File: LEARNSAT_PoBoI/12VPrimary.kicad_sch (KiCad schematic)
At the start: 17 parts, among them Q3 SI7164DP-T1-GE3, U13 INA219AIDCNR, U18 LTC4231IUD-2#TRPBF

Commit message: Changed diode D?1 to D23 as a git test
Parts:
- renumbered D?1 to D23
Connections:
- net 12V_EnableP: now also D23.2 (A); no longer D23.1 (K)
- net GND: now also D23.1 (K); no longer D23.2 (A)

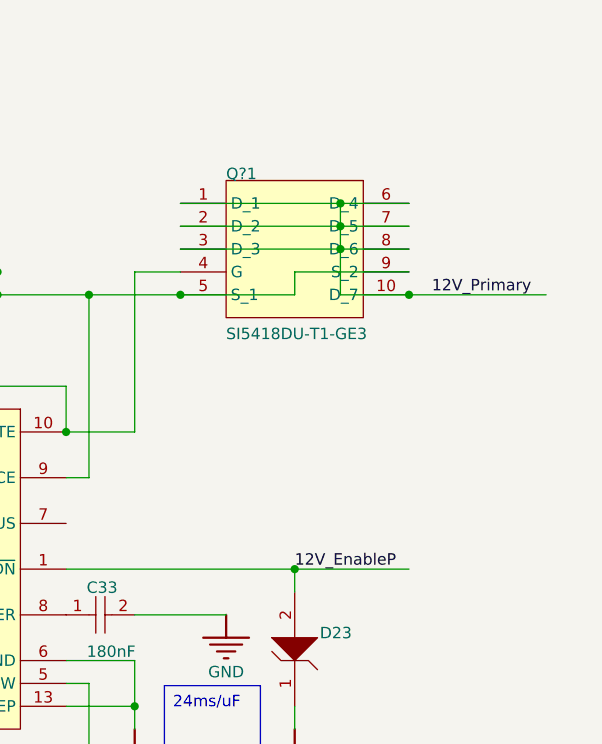
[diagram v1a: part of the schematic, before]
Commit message: Small global net changes
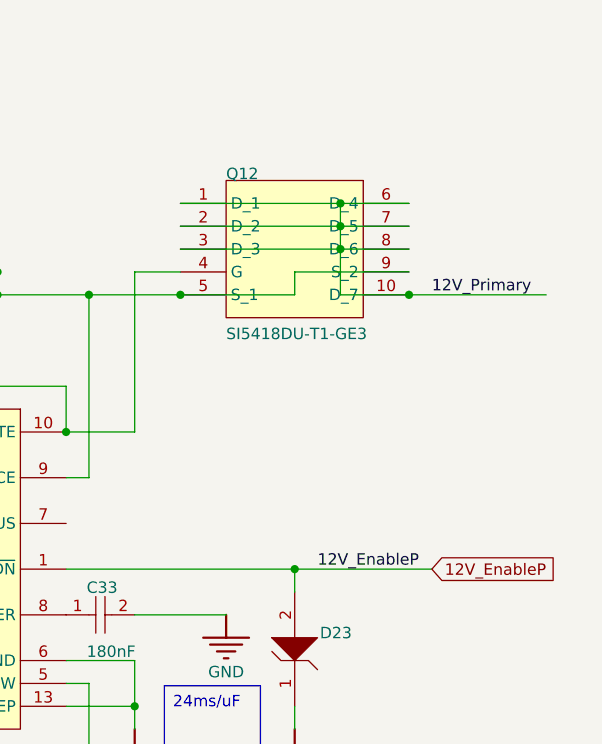
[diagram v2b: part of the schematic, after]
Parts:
- renumbered Q?1 to Q12
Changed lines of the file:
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@@
 	)
 	(junction
-		(at 167.64 149.86)
-		(diameter 0)
-		(color 0 0 0 0)
-	)
-	(junction
 		(at 99.06 45.72)
 		(diameter 0)
@@
 	)
 	(junction
+		(at 167.64 149.86)
+		(diameter 0)
+		(color 0 0 0 0)
+	)
+	(junction
 		(at 149.86 165.1)
 		(diameter 0)
@@
 	(wire
 		(pts
-			(xy 167.64 149.86) (xy 180.34 149.86)
+			(xy 167.64 149.86) (xy 182.88 149.86)
 		)
 		(stroke
@@
 	)
 	(label "12V_EnableP"
-		(at 167.64 149.86 0)
+		(at 170.18 149.86 0)
 		(effects
 			(font
@@
 		)
 	)
+	(global_label "12V_EnableP"
+		(shape input)
+		(at 182.88 149.86 0)
+		(fields_autoplaced yes)
+		(effects
+			(font
+				(size 1.27 1.27)
+			)
+			(justify left)
+		)
+		(property "Intersheetrefs" "${INTERSHEET_REFS}"
+			(at 197.9602 149.86 0)
+			(hide yes)
+			(show_name no)
+			(do_not_autoplace no)
+			(effects
+				(font
+					(size 1.27 1.27)
+				)
+				(justify left)
+			)
+		)
+	)
 	(symbol
 		(lib_id "UGA SSRL Hardware Team:root_0_94c330ae140e2337d879337fe7aaeec_UGA SSRL Hardware Team")
@@
 		(in_pos_files yes)
 		(dnp no)
-		(property "Reference" "Q?1"
+		(property "Reference" "Q12"
 			(at 160.02 106.68 0)
 			(show_name no)
@@
 			(project "LEARNSAT_POBOY_v3.2.0"
 				(path "/31302da5-a970-4b2b-aa05-afcd06cb9d09/2029a850-3e48-491b-a9aa-1537ac8442d4"
-					(reference "Q?1")
+					(reference "Q12")
 					(unit 1)
 				)

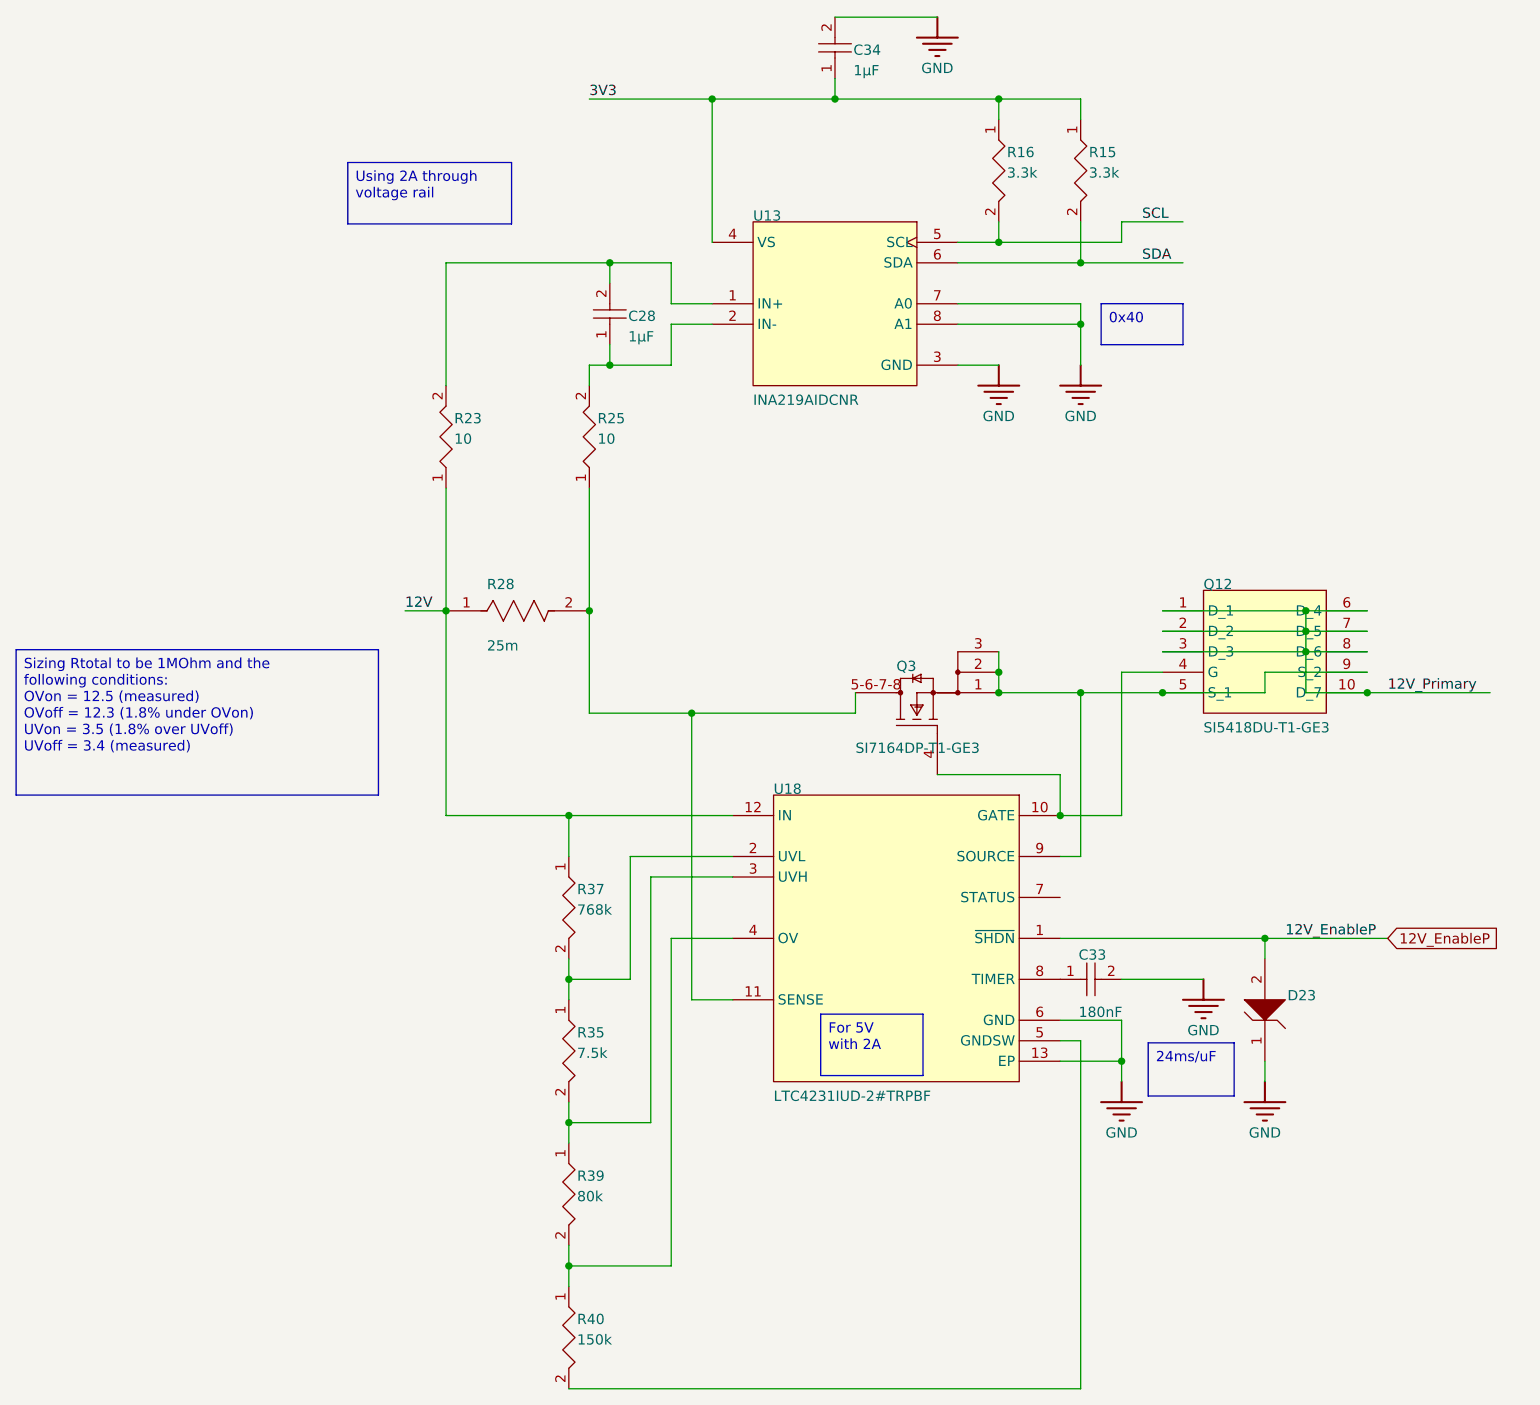
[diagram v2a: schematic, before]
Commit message: Replaced local nets with global and left local nets intact
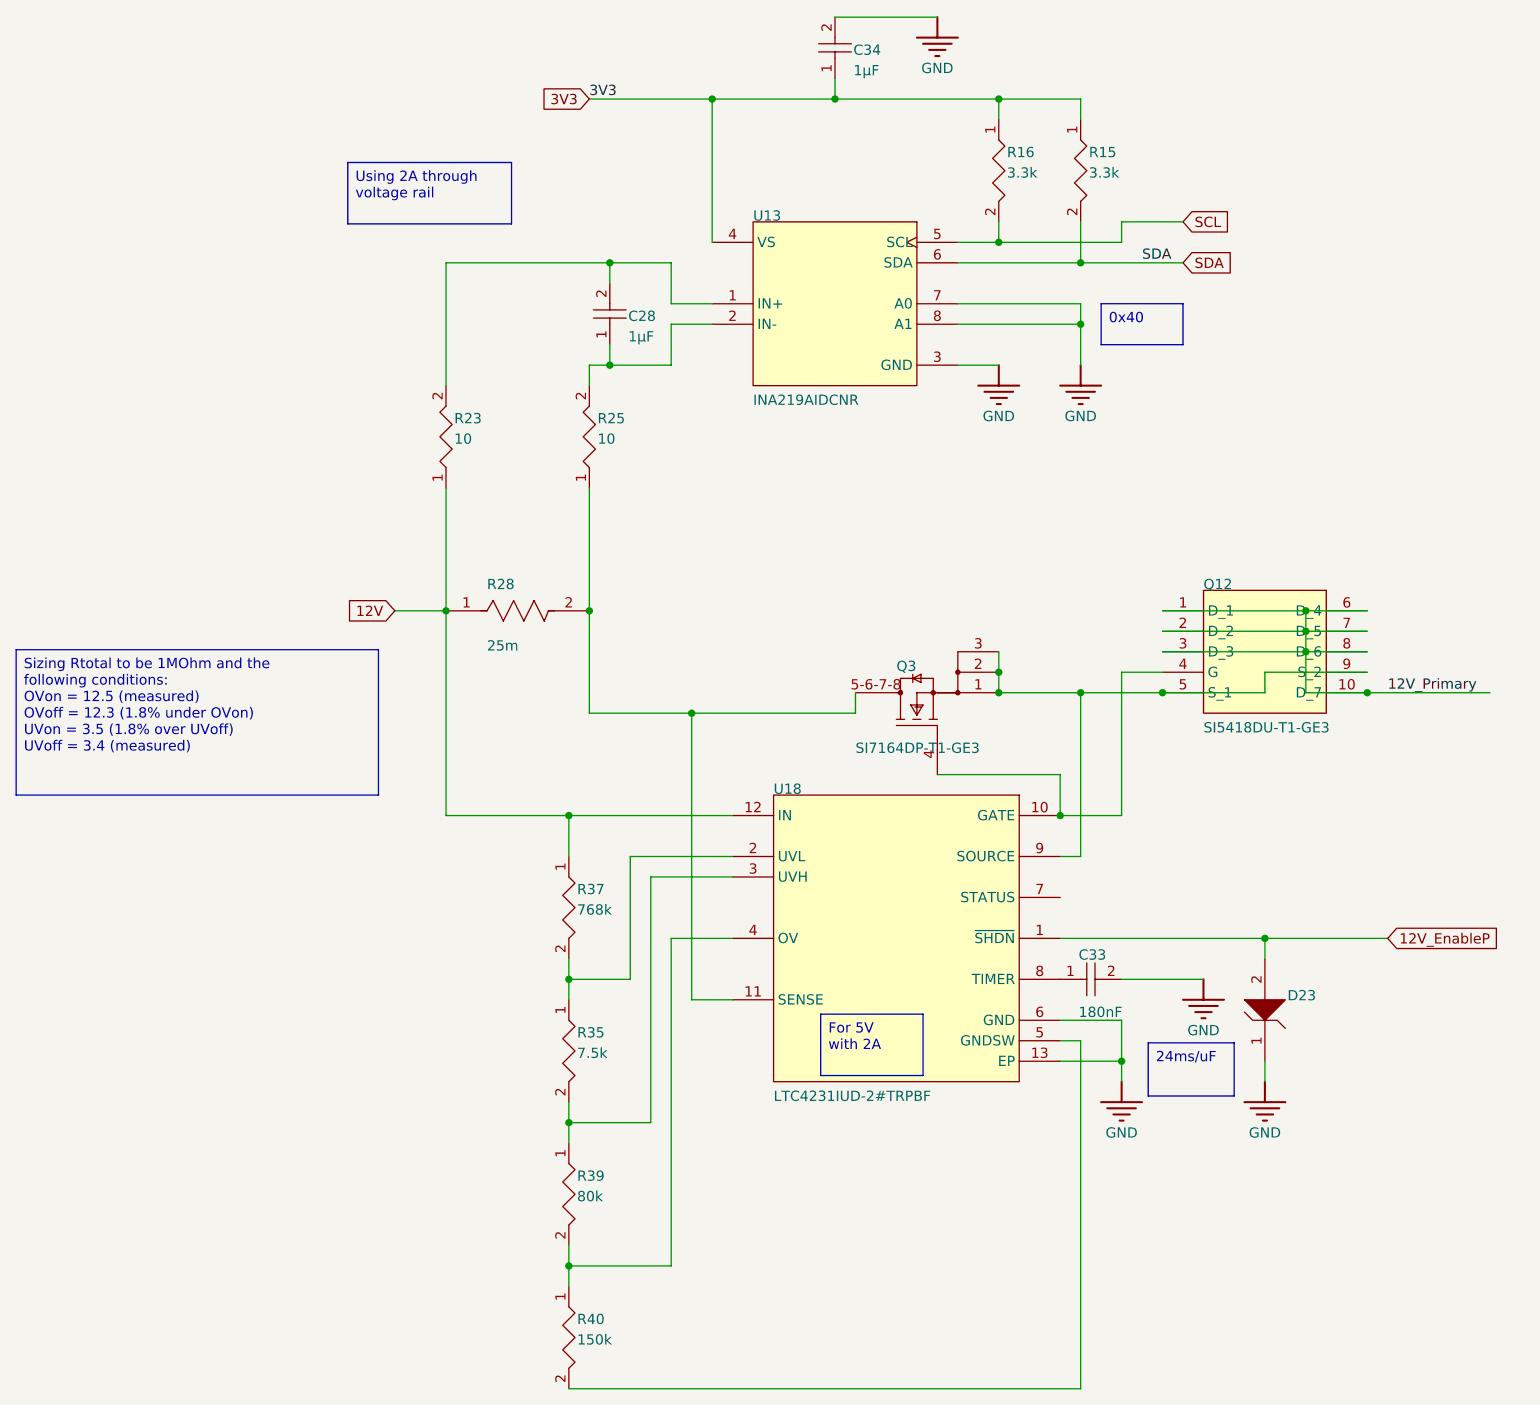
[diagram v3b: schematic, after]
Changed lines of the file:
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@@
 	(wire
 		(pts
-			(xy 60.96 109.22) (xy 66.04 109.22)
+			(xy 59.69 109.22) (xy 66.04 109.22)
 		)
 		(stroke
@@
 		)
 	)
-	(label "12V"
-		(at 60.96 109.22 0)
+	(label "SDA"
+		(at 152.4 66.04 0)
 		(effects
 			(font
@@
 		)
 	)
-	(label "SCL"
-		(at 152.4 60.96 0)
+	(label "3V3"
+		(at 83.82 45.72 0)
 		(effects
 			(font
@@
 		)
 	)
-	(label "SDA"
-		(at 152.4 66.04 0)
+	(label "12V_Primary"
+		(at 182.88 119.38 0)
 		(effects
 			(font
@@
 		)
 	)
-	(label "3V3"
-		(at 83.82 45.72 0)
+	(global_label "SCL"
+		(shape input)
+		(at 157.48 60.96 0)
+		(fields_autoplaced yes)
 		(effects
 			(font
 				(size 1.27 1.27)
 			)
-			(justify left bottom)
+			(justify left)
+		)
+		(property "Intersheetrefs" "${INTERSHEET_REFS}"
+			(at 163.9728 60.96 0)
+			(hide yes)
+			(show_name no)
+			(do_not_autoplace no)
+			(effects
+				(font
+					(size 1.27 1.27)
+				)
+				(justify left)
+			)
 		)
 	)
-	(label "12V_Primary"
-		(at 182.88 119.38 0)
+	(global_label "3V3"
+		(shape input)
+		(at 83.82 45.72 180)
+		(fields_autoplaced yes)
 		(effects
 			(font
 				(size 1.27 1.27)
 			)
-			(justify left bottom)
+			(justify right)
+		)
+		(property "Intersheetrefs" "${INTERSHEET_REFS}"
+			(at 77.3272 45.72 0)
+			(hide yes)
+			(show_name no)
+			(do_not_autoplace no)
+			(effects
+				(font
+					(size 1.27 1.27)
+				)
+				(justify right)
+			)
 		)
 	)
-	(label "12V_EnableP"
-		(at 170.18 149.86 0)
+	(global_label "SDA"
+		(shape input)
+		(at 157.48 66.04 0)
+		(fields_autoplaced yes)
 		(effects
 			(font
 				(size 1.27 1.27)
 			)
-			(justify left bottom)
+			(justify left)
+		)
+		(property "Intersheetrefs" "${INTERSHEET_REFS}"
+			(at 164.0333 66.04 0)
+			(hide yes)
+			(show_name no)
+			(do_not_autoplace no)
+			(effects
+				(font
+					(size 1.27 1.27)
+				)
+				(justify left)
+			)
 		)
 	)
@@
 			)
 		)
+	)
+	(global_label "12V"
+		(shape input)
+		(at 59.69 109.22 180)
+		(fields_autoplaced yes)
+		(effects
+			(font
+				(size 1.27 1.27)
+			)
+			(justify right)
+		)
+		(property "Intersheetrefs" "${INTERSHEET_REFS}"
+			(at 53.1972 109.22 0)
+			(hide yes)
+			(show_name no)
+			(do_not_autoplace no)
+			(effects
+				(font
+					(size 1.27 1.27)
+				)
+				(justify right)
+			)
+		)

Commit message: Added footprints
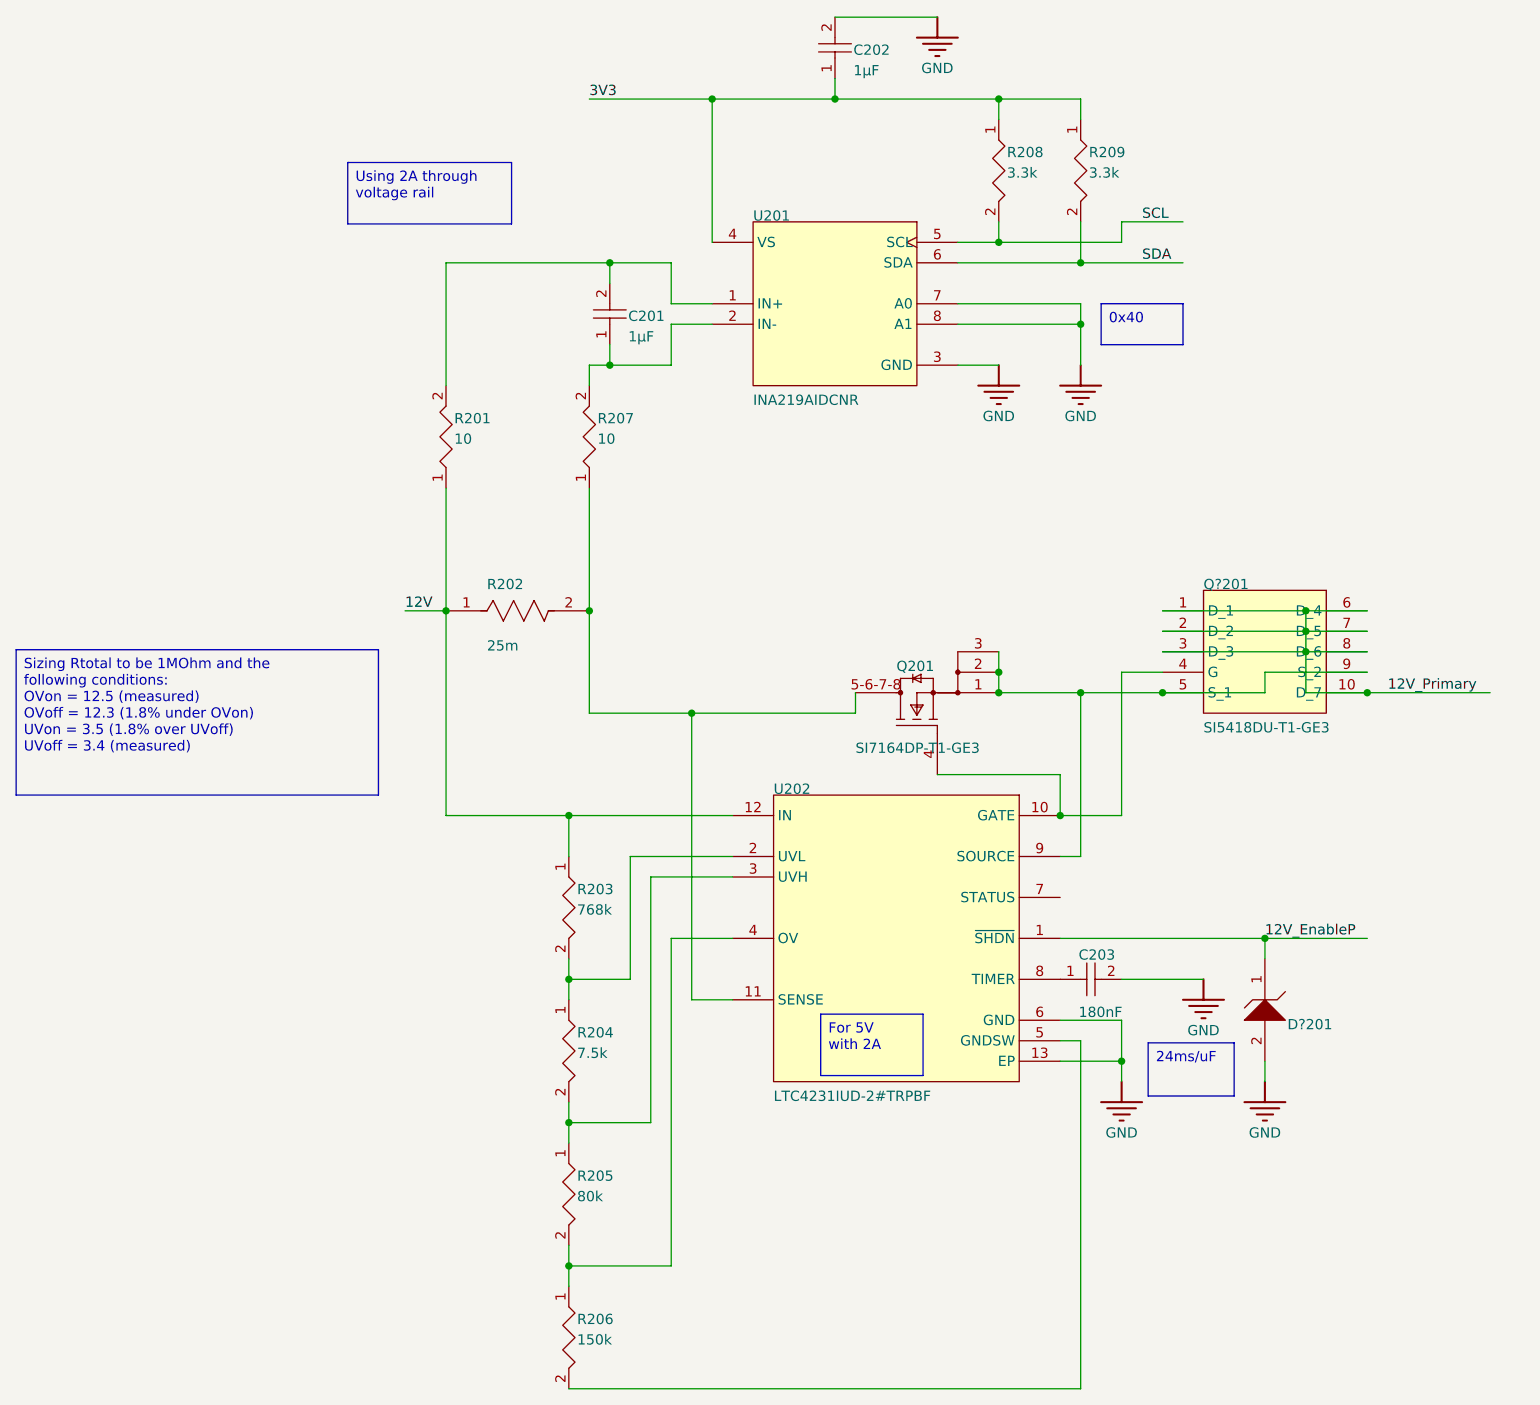
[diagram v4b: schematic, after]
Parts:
- C201: renamed from C28; footprint CAPC1608X90X40LL10T20 -> Capacitor_SMD:C_0603_1608Metric
- C202: renamed from C34; footprint CAPC1608X90X35ML15T15 -> Capacitor_SMD:C_0603_1608Metric
- C203: renamed from C33; footprint FP-C0805C-DN-IPC_A -> Capacitor_SMD:C_0805_2012Metric
- D?201: renamed from D23; footprint ONSC-SOD-323-2-477-02_V -> Diode_SMD:D_SOD-323
- Q201: renamed from Q3; footprint Vishay_S17-0173-SINGLE_MFG -> Package_SO:Vishay_PowerPAK_1212-8_Single
- Q?201: renamed from Q12; footprint SI5418DU-T1-GE3-Footprint-1 -> Package_SO:Vishay_PowerPAK_1212-8_Single
- R201: renamed from R23; footprint RESC0402(1005)_L -> Resistor_SMD:R_0402_1005Metric
- R202: renamed from R28; footprint FP-CSR1206-IPC_C -> Resistor_SMD:R_1206_3216Metric
- R203: renamed from R37; footprint RESC0402(1005)_L -> Resistor_SMD:R_0402_1005Metric
- R204: renamed from R35; footprint FP-CRCW1206-e3-IPC_A -> Resistor_SMD:R_1206_3216Metric
- R205: renamed from R39; footprint FP-PTN0603-IPC_B -> Resistor_SMD:R_0603_1608Metric
- R206: renamed from R40; footprint FP-RT1206-IPC_C -> Resistor_SMD:R_1206_3216Metric
- R207: renamed from R25; footprint RESC0402(1005)_L -> Resistor_SMD:R_0402_1005Metric
- R208: renamed from R16; footprint FP-CRCW1210-e3-IPC_C -> Resistor_SMD:R_1210_3225Metric
- R209: renamed from R15; footprint FP-CRCW1210-e3-IPC_C -> Resistor_SMD:R_1210_3225Metric
- U201: renamed from U13; footprint FP-DCN0008A-IPC_A -> INA219AIDCNR:SOT65P280X145-8N
- U202: renamed from U18; footprint FP-UD-12-05-08-1855-IPC_A -> LTC4231IUD-2_TRPBF:QFN50P300X300X80-13N
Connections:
- net 12V_EnableP: now also D?201.1 (K); no longer D?201.2 (A)
- net GND: now also D?201.2 (A); no longer D?201.1 (K)

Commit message: Add files via upload
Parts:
- C28: renamed from C201; footprint Capacitor_SMD:C_0603_1608Metric -> CAPC1608X90X40LL10T20
- C33: renamed from C203; footprint Capacitor_SMD:C_0805_2012Metric -> FP-C0805C-DN-IPC_A
- C34: renamed from C202; footprint Capacitor_SMD:C_0603_1608Metric -> CAPC1608X90X35ML15T15
- D23: renamed from D?201; footprint Diode_SMD:D_SOD-323 -> ONSC-SOD-323-2-477-02_V
- Q12: renamed from Q?201; footprint Package_SO:Vishay_PowerPAK_1212-8_Single -> SI5418DU-T1-GE3-Footprint-1
- Q3: renamed from Q201; footprint Package_SO:Vishay_PowerPAK_1212-8_Single -> Vishay_S17-0173-SINGLE_MFG
- R15: renamed from R209; footprint Resistor_SMD:R_1210_3225Metric -> FP-CRCW1210-e3-IPC_C
- R16: renamed from R208; footprint Resistor_SMD:R_1210_3225Metric -> FP-CRCW1210-e3-IPC_C
- R23: renamed from R201; footprint Resistor_SMD:R_0402_1005Metric -> RESC0402(1005)_L
- R25: renamed from R207; footprint Resistor_SMD:R_0402_1005Metric -> RESC0402(1005)_L
- R28: renamed from R202; footprint Resistor_SMD:R_1206_3216Metric -> FP-CSR1206-IPC_C
- R35: renamed from R204; footprint Resistor_SMD:R_1206_3216Metric -> FP-CRCW1206-e3-IPC_A
- R37: renamed from R203; footprint Resistor_SMD:R_0402_1005Metric -> RESC0402(1005)_L
- R39: renamed from R205; footprint Resistor_SMD:R_0603_1608Metric -> FP-PTN0603-IPC_B
- R40: renamed from R206; footprint Resistor_SMD:R_1206_3216Metric -> FP-RT1206-IPC_C
- U13: renamed from U201; footprint INA219AIDCNR:SOT65P280X145-8N -> FP-DCN0008A-IPC_A
- U18: renamed from U202; footprint LTC4231IUD-2_TRPBF:QFN50P300X300X80-13N -> FP-UD-12-05-08-1855-IPC_A
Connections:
- net 12V_EnableP: now also D23.2 (A); no longer D23.1 (K)
- net GND: now also D23.1 (K); no longer D23.2 (A)
